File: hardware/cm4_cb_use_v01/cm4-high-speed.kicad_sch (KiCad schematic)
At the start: 5 parts, among them U2 TPD2EUSB30

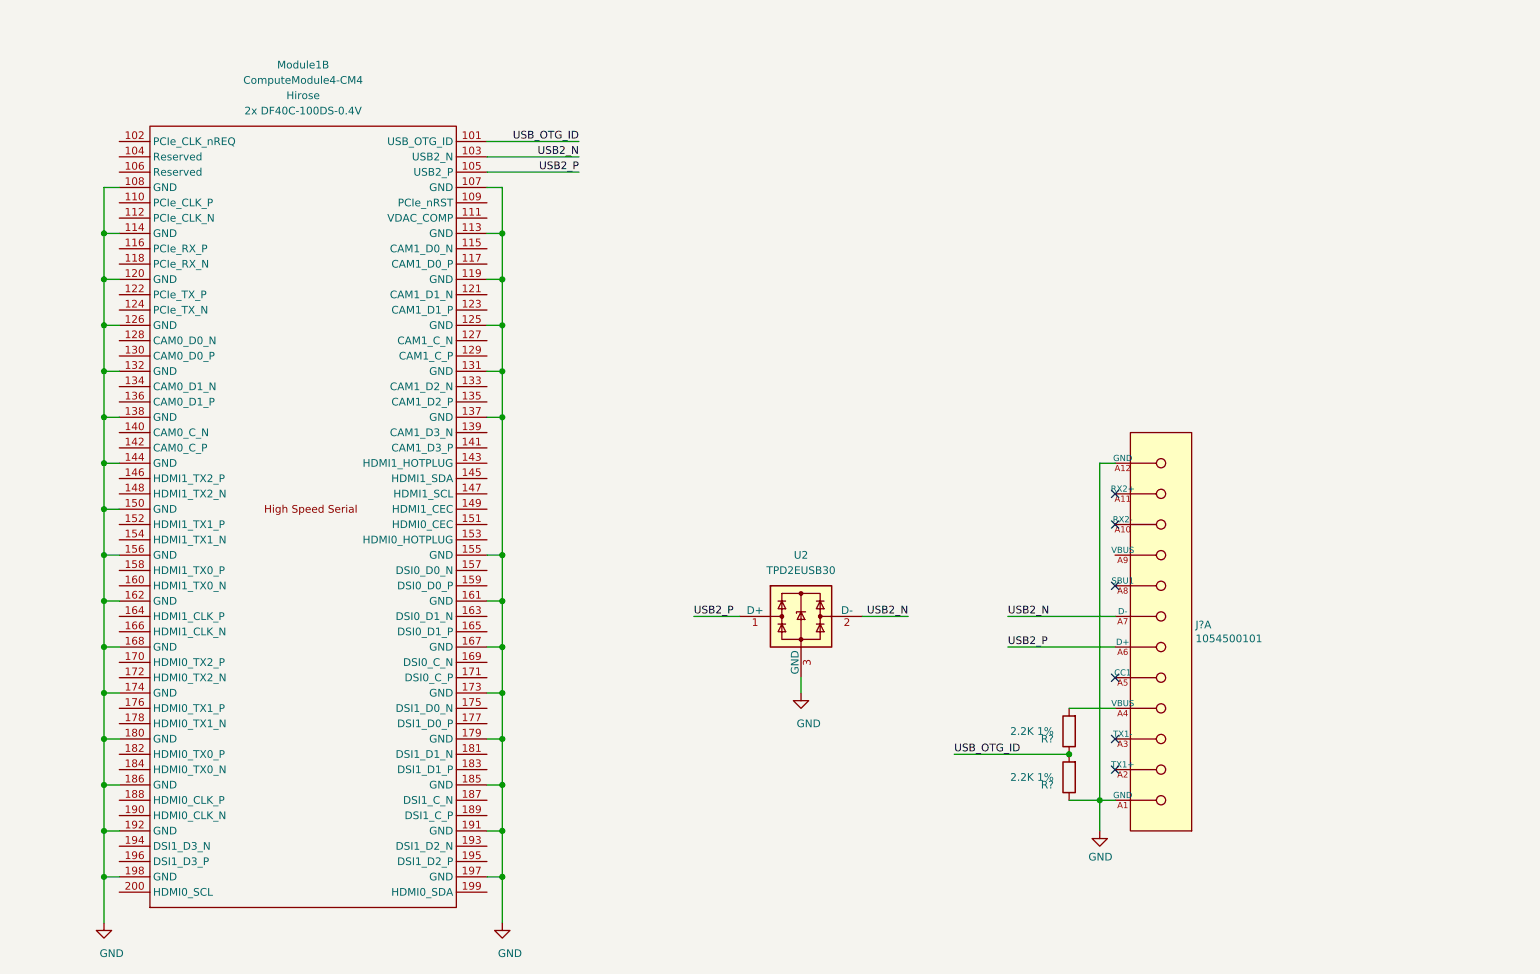
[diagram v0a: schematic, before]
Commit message: added usb-c and hdmi
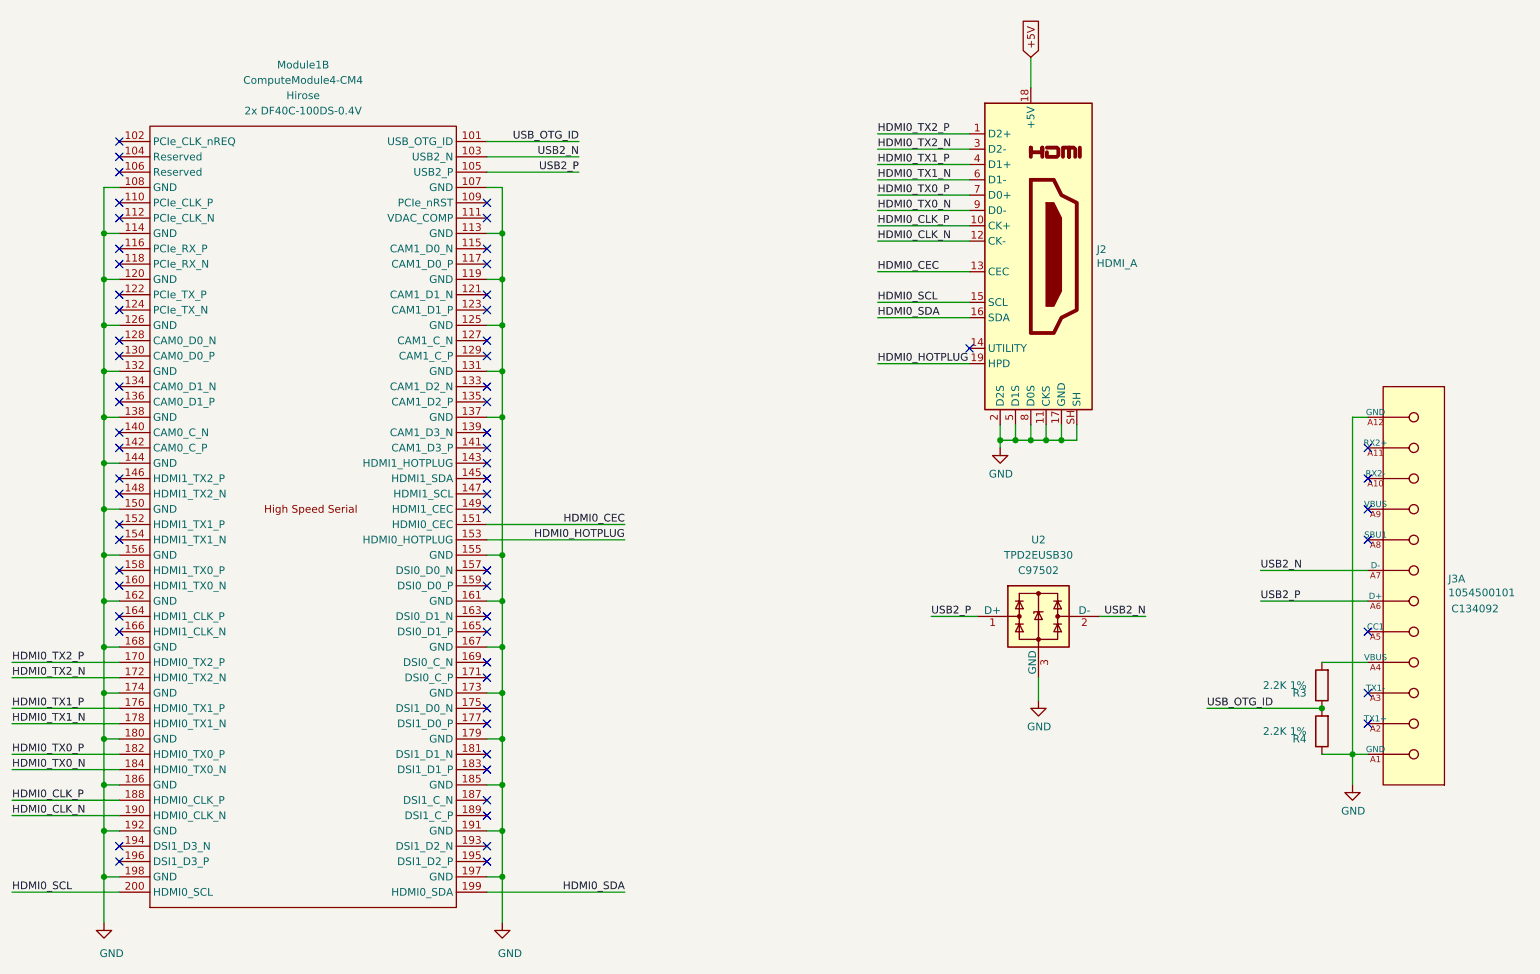
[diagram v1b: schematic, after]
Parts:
- added J2: HDMI_A, symbol Connector:HDMI_A
- J3: renamed from J?; footprint Molex-1054500101-* -> (none); LCSC (none) -> C134092
- Module1: LCSC (none) -> C597931
- U2: Digi-Key_PN 296-25509-1-ND -> (none); LCSC (none) -> C97502
- gave numbers to parts that had none: 2
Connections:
- net GND: now also J2.11 (CKS), J2.17 (GND), J2.2 (D2S), J2.5 (D1S), J2.8 (D0S), J2.SH
- net HDMI0_CEC: now reaches Module1.151 (HDMI0_CEC)
- net HDMI0_CEC: now also J2.13 (CEC)
- net HDMI0_HOTPLUG: now reaches Module1.153 (HDMI0_HOTPLUG)
- net HDMI0_HOTPLUG: now also J2.19 (HPD)
- net HDMI0_TX2_P: now reaches Module1.170 (HDMI0_TX2_P)
- net HDMI0_TX2_P: now also J2.1 (D2+)
- net HDMI0_TX2_N: now reaches Module1.172 (HDMI0_TX2_N)
- net HDMI0_TX2_N: now also J2.3 (D2-)
- net HDMI0_TX1_P: now reaches Module1.176 (HDMI0_TX1_P)
- net HDMI0_TX1_P: now also J2.4 (D1+)
- net HDMI0_TX1_N: now reaches Module1.178 (HDMI0_TX1_N)
- net HDMI0_TX1_N: now also J2.6 (D1-)
- net HDMI0_TX0_P: now reaches Module1.182 (HDMI0_TX0_P)
- net HDMI0_TX0_P: now also J2.7 (D0+)
- net HDMI0_TX0_N: now reaches Module1.184 (HDMI0_TX0_N)
- net HDMI0_TX0_N: now also J2.9 (D0-)
- net HDMI0_CLK_P: now reaches Module1.188 (HDMI0_CLK_P)
- net HDMI0_CLK_P: now also J2.10 (CK+)
- net HDMI0_CLK_N: now reaches Module1.190 (HDMI0_CLK_N)
- net HDMI0_CLK_N: now also J2.12 (CK-)
- net HDMI0_SDA: now reaches Module1.199 (HDMI0_SDA)
- net HDMI0_SDA: now also J2.16 (SDA)
- net HDMI0_SCL: now reaches Module1.200 (HDMI0_SCL)
- net HDMI0_SCL: now also J2.15 (SCL)
- new net +5V: J2.18 (+5V)
- no-connect marks 6 -> 63
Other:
- moved on the sheet: J3A, R3, R4, U2

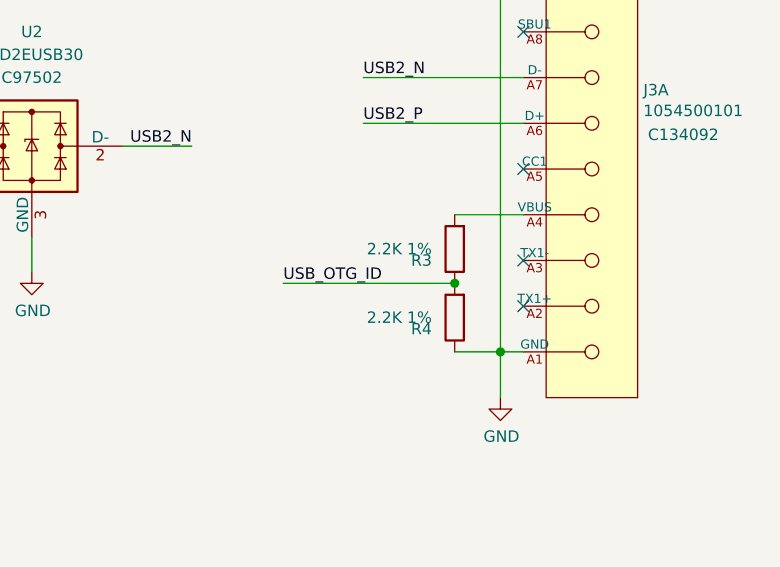
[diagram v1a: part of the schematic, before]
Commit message: added some 3d models
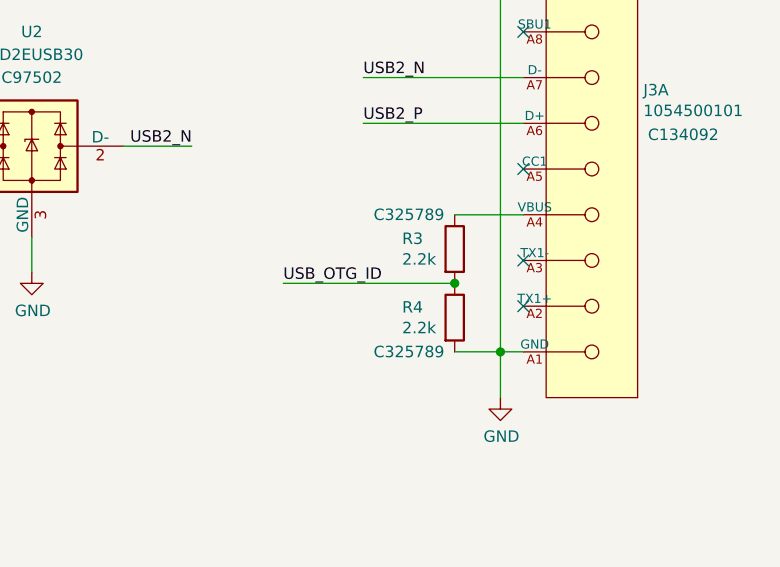
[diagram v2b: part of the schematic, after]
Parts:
- J2: footprint (none) -> SFONG_HDMI:SOFNG_HDMI; LCSC C111617 -> C111617
- J3: footprint (none) -> MOLEX_1054500101_usb_c:Molex-1054500101-MFG
- R3, R4: value 2.2K 1% -> 2.2k; footprint Resistor_SMD:R_0603_1608Metric_Pad0.98x0.95mm_HandSolder -> Resistor_SMD:R_0805_2012Metric; Digi-Key_PN 311-2.20KHRCT-ND -> (none); LCSC (none) -> C325789; MPN RC0603FR-072K2L -> (none); Manufacturer Yageo -> (none)
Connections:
- net GND: now also R4.2; no longer R4.1
- net USB_OTG_ID: now also R3.2, R4.1; no longer R3.1, R4.2
- net at J3.A4 (VBUS): now also R3.1; no longer R3.2
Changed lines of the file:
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@@
     (pin "1")
   )
-  (symbol (lib_id "Device:R") (at 242.57 135.89 180) (unit 1)
+  (symbol (lib_id "Device:R") (at 242.57 135.89 0) (unit 1)
     (in_bom yes) (on_board yes)
-    (property "Reference" "R3" (id 0) (at 240.03 137.16 0)
+    (property "Reference" "R3" (id 0) (at 236.7281 134.7406 0)
       (effects (font (size 1.27 1.27)) (justify left))
     )
-    (property "Value" "2.2K 1%" (id 1) (at 240.03 135.89 0)
+    (property "Value" "2.2k" (id 1) (at 236.728 137.039 0)
       (effects (font (size 1.27 1.27)) (justify left))
     )
-    (property "Footprint" "Resistor_SMD:R_0603_1608Metric_Pad0.98x0.95mm_HandSolder" (id 2) (at 244.348 135.89 90)
+    (property "Footprint" "Resistor_SMD:R_0805_2012Metric" (id 2) (at 240.792 135.89 90)
       (effects (font (size 1.27 1.27)) hide)
     )
-    (property "Datasheet" "~" (id 3) (at 242.57 135.89 0)
+    (property "Datasheet" "https://datasheet.lcsc.com/szlcsc/1912111437_TyoHM-RMC08052-2K5-N_C325789.pdf" (id 3) (at 242.57 135.89 0)
       (effects (font (size 1.27 1.27)) hide)
     )
-    (property "Manufacturer" "Yageo" (id 4) (at 242.57 135.89 0)
-      (effects (font (size 1.27 1.27)) hide)
-    )
-    (property "MPN" "RC0603FR-072K2L" (id 5) (at 242.57 135.89 0)
-      (effects (font (size 1.27 1.27)) hide)
-    )
-    (property "Digi-Key_PN" "311-2.20KHRCT-ND" (id 6) (at 242.57 135.89 0)
-      (effects (font (size 1.27 1.27)) hide)
-    )
+    (property "LCSC" "C325789" (id 4) (at 237.49 132.08 0))
     (pin "1")
     (pin "2")
   )
-  (symbol (lib_id "Device:R") (at 242.57 143.51 180) (unit 1)
+  (symbol (lib_id "Device:R") (at 242.57 143.51 0) (unit 1)
     (in_bom yes) (on_board yes)
-    (property "Reference" "R4" (id 0) (at 240.03 144.78 0)
+    (property "Reference" "R4" (id 0) (at 236.7281 142.3606 0)
       (effects (font (size 1.27 1.27)) (justify left))
     )
-    (property "Value" "2.2K 1%" (id 1) (at 240.03 143.51 0)
+    (property "Value" "2.2k" (id 1) (at 236.728 144.659 0)
       (effects (font (size 1.27 1.27)) (justify left))
     )
-    (property "Footprint" "Resistor_SMD:R_0603_1608Metric_Pad0.98x0.95mm_HandSolder" (id 2) (at 244.348 143.51 90)
+    (property "Footprint" "Resistor_SMD:R_0805_2012Metric" (id 2) (at 240.792 143.51 90)
       (effects (font (size 1.27 1.27)) hide)
     )
-    (property "Datasheet" "~" (id 3) (at 242.57 143.51 0)
+    (property "Datasheet" "https://datasheet.lcsc.com/szlcsc/1912111437_TyoHM-RMC08052-2K5-N_C325789.pdf" (id 3) (at 242.57 143.51 0)
       (effects (font (size 1.27 1.27)) hide)
     )
-    (property "Manufacturer" "Yageo" (id 4) (at 242.57 143.51 0)
-      (effects (font (size 1.27 1.27)) hide)
-    )
-    (property "MPN" "RC0603FR-072K2L" (id 5) (at 242.57 143.51 0)
-      (effects (font (size 1.27 1.27)) hide)
-    )
-    (property "Digi-Key_PN" "311-2.20KHRCT-ND" (id 6) (at 242.57 143.51 0)
-      (effects (font (size 1.27 1.27)) hide)
-    )
+    (property "LCSC" "C325789" (id 4) (at 237.49 147.32 0))
     (pin "1")
     (pin "2")
@@
       (effects (font (size 1.27 1.27)) (justify right))
     )
-    (property "Footprint" "" (id 2) (at 247.65 160.02 0)
+    (property "Footprint" "MOLEX_1054500101_usb_c:Molex-1054500101-MFG" (id 2) (at 247.65 160.02 0)
       (effects (font (size 1.27 1.27)) (justify left) hide)
     )
@@
       (effects (font (size 1.27 1.27)) (justify left))
     )
-    (property "Footprint" "" (id 2) (at 194.945 64.77 0)
+    (property "Footprint" "SFONG_HDMI:SOFNG_HDMI" (id 2) (at 194.945 64.77 0)
       (effects (font (size 1.27 1.27)) hide)
     )
@@
       (effects (font (size 1.27 1.27)) hide)
     )
-    (property "LCSC" " 	C111617" (id 4) (at 194.31 64.77 0)
+    (property "LCSC" "C111617" (id 4) (at 194.31 64.77 0)
       (effects (font (size 1.27 1.27)) hide)
     )

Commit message: updated
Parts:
- J2: footprint SFONG_HDMI:SOFNG_HDMI -> MOLEX_1054500101_usb_c:molex_hdmi
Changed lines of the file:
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@@
       (effects (font (size 1.27 1.27)) (justify left))
     )
-    (property "Footprint" "SFONG_HDMI:SOFNG_HDMI" (id 2) (at 194.945 64.77 0)
+    (property "Footprint" "MOLEX_1054500101_usb_c:molex_hdmi" (id 2) (at 194.945 64.77 0)
       (effects (font (size 1.27 1.27)) hide)
     )
